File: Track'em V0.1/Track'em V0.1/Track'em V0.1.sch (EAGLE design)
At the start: 34 parts, among them IC1 SAM-M8Q, J1 CORTEX_DEBUG_PTH, U2 3.3V/150mA

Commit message: track'em updates
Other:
- moved on the sheet: C10, C11, C12, C13, C14, C15, C3, C4, C5, C6, C7, C8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

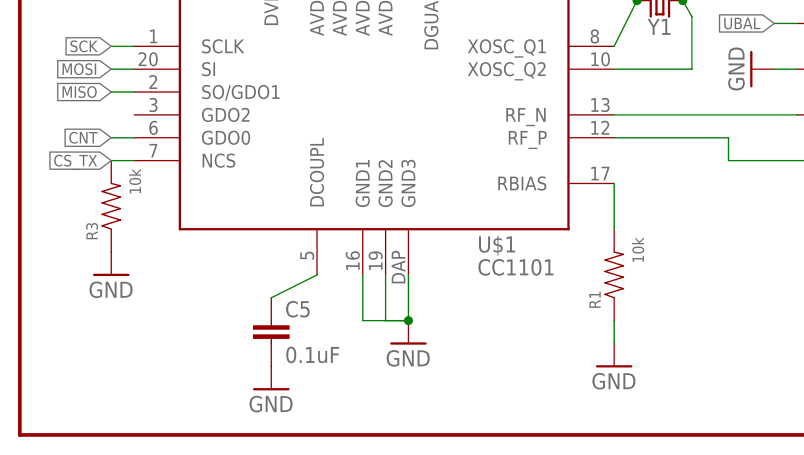
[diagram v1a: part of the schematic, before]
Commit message: boards sent to fab
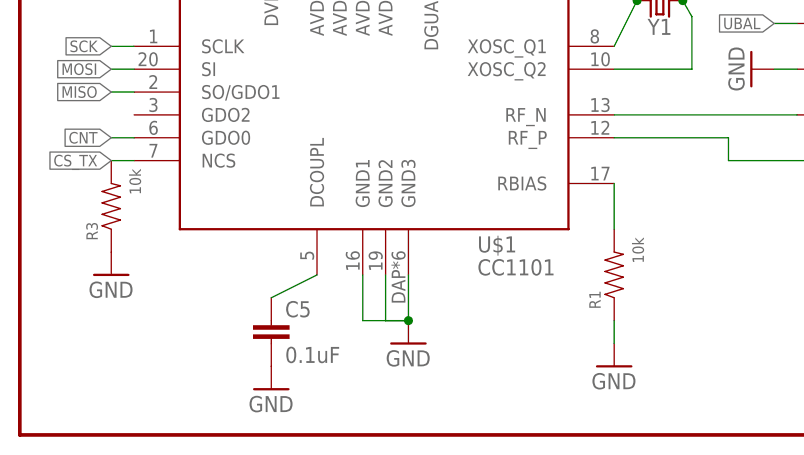
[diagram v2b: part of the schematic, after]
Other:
- moved on the sheet: U$1

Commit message: this Track'em sent to fab
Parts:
- added C16: 10uF, SparkFun-Capacitors:10UF-6.3V-20%(0603)(TANT)"
- C10, C7: value 0.1uF -> 10nF
- C11, C12, C9: value 0.1uF -> 220pF
- C13: value 0.1uF -> 12pF
- C14: value 0.1uF -> 15pF
- C5, C6: value 0.1uF -> 100nF
- R1: value 10k -> 56k
- Y1: value (none) -> 26MHz
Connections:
- net 3.3V: now also C16.+, R3.1
- net GND: now also C16.-; no longer R3.1

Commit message: tracking message parsed from GPS
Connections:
- net USART_RX: now also U$2.PA24(USB_D-/SER1:2); no longer U$2.PA25(USB_D+/SER1:3)
- net USART_TX: now also U$2.PA25(USB_D+/SER1:3); no longer U$2.PA24(USB_D-/SER1:2)
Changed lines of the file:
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@@
 <grid distance="0.1" unitdist="inch" unit="inch" style="lines" multiple="1" display="no" altdistance="0.01" altunitdist="inch" altunit="inch"/>
 <layers>
-<layer number="1" name="Top" color="4" fill="1" visible="yes" active="no"/>
-<layer number="2" name="Route2" color="1" fill="3" visible="yes" active="no"/>
-<layer number="3" name="Route3" color="4" fill="3" visible="yes" active="no"/>
-<layer number="4" name="Route4" color="1" fill="4" visible="yes" active="no"/>
-<layer number="5" name="Route5" color="4" fill="4" visible="yes" active="no"/>
-<layer number="6" name="Route6" color="1" fill="8" visible="yes" active="no"/>
-<layer number="7" name="Route7" color="4" fill="8" visible="yes" active="no"/>
-<layer number="8" name="Route8" color="1" fill="2" visible="yes" active="no"/>
-<layer number="9" name="Route9" color="4" fill="2" visible="yes" active="no"/>
-<layer number="10" name="Route10" color="1" fill="7" visible="yes" active="no"/>
-<layer number="11" name="Route11" color="4" fill="7" visible="yes" active="no"/>
-<layer number="12" name="Route12" color="1" fill="5" visible="yes" active="no"/>
-<layer number="13" name="Route13" color="4" fill="5" visible="yes" active="no"/>
-<layer number="14" name="Route14" color="1" fill="6" visible="yes" active="no"/>
-<layer number="15" name="Route15" color="4" fill="6" visible="yes" active="no"/>
-<layer number="16" name="Bottom" color="1" fill="1" visible="yes" active="no"/>
-<layer number="17" name="Pads" color="2" fill="1" visible="yes" active="no"/>
-<layer number="18" name="Vias" color="2" fill="1" visible="yes" active="no"/>
-<layer number="19" name="Unrouted" color="6" fill="1" visible="yes" active="no"/>
-<layer number="20" name="Dimension" color="24" fill="1" visible="yes" active="no"/>
-<layer number="21" name="tPlace" color="7" fill="1" visible="yes" active="no"/>
-<layer number="22" name="bPlace" color="7" fill="1" visible="yes" active="no"/>
-<layer number="23" name="tOrigins" color="15" fill="1" visible="yes" active="no"/>
-<layer number="24" name="bOrigins" color="15" fill="1" visible="yes" active="no"/>
-<layer number="25" name="tNames" color="7" fill="1" visible="yes" active="no"/>
-<layer number="26" name="bNames" color="7" fill="1" visible="yes" active="no"/>
-<layer number="27" name="tValues" color="7" fill="1" visible="yes" active="no"/>
-<layer number="28" name="bValues" color="7" fill="1" visible="yes" active="no"/>
+<layer number="1" name="Top" color="4" fill="1" visible="no" active="no"/>
+<layer number="2" name="Route2" color="1" fill="3" visible="no" active="no"/>
+<layer number="3" name="Route3" color="4" fill="3" visible="no" active="no"/>
+<layer number="4" name="Route4" color="1" fill="4" visible="no" active="no"/>
+<layer number="5" name="Route5" color="4" fill="4" visible="no" active="no"/>
+<layer number="6" name="Route6" color="1" fill="8" visible="no" active="no"/>
+<layer number="7" name="Route7" color="4" fill="8" visible="no" active="no"/>
+<layer number="8" name="Route8" color="1" fill="2" visible="no" active="no"/>
+<layer number="9" name="Route9" color="4" fill="2" visible="no" active="no"/>
+<layer number="10" name="Route10" color="1" fill="7" visible="no" active="no"/>
+<layer number="11" name="Route11" color="4" fill="7" visible="no" active="no"/>
+<layer number="12" name="Route12" color="1" fill="5" visible="no" active="no"/>
+<layer number="13" name="Route13" color="4" fill="5" visible="no" active="no"/>
+<layer number="14" name="Route14" color="1" fill="6" visible="no" active="no"/>
+<layer number="15" name="Route15" color="4" fill="6" visible="no" active="no"/>
+<layer number="16" name="Bottom" color="1" fill="1" visible="no" active="no"/>
+<layer number="17" name="Pads" color="2" fill="1" visible="no" active="no"/>
+<layer number="18" name="Vias" color="2" fill="1" visible="no" active="no"/>
+<layer number="19" name="Unrouted" color="6" fill="1" visible="no" active="no"/>
+<layer number="20" name="Dimension" color="24" fill="1" visible="no" active="no"/>
+<layer number="21" name="tPlace" color="7" fill="1" visible="no" active="no"/>
+<layer number="22" name="bPlace" color="7" fill="1" visible="no" active="no"/>
+<layer number="23" name="tOrigins" color="15" fill="1" visible="no" active="no"/>
+<layer number="24" name="bOrigins" color="15" fill="1" visible="no" active="no"/>
+<layer number="25" name="tNames" color="7" fill="1" visible="no" active="no"/>
+<layer number="26" name="bNames" color="7" fill="1" visible="no" active="no"/>
+<layer number="27" name="tValues" color="7" fill="1" visible="no" active="no"/>
+<layer number="28" name="bValues" color="7" fill="1" visible="no" active="no"/>
 <layer number="29" name="tStop" color="7" fill="3" visible="no" active="no"/>
 <layer number="30" name="bStop" color="7" fill="6" visible="no" active="no"/>
@@
 <layer number="35" name="tGlue" color="7" fill="4" visible="no" active="no"/>
 <layer number="36" name="bGlue" color="7" fill="5" visible="no" active="no"/>
-<layer number="37" name="tTest" color="7" fill="1" visible="yes" active="no"/>
-<layer number="38" name="bTest" color="7" fill="1" visible="yes" active="no"/>
+<layer number="37" name="tTest" color="7" fill="1" visible="no" active="no"/>
+<layer number="38" name="bTest" color="7" fill="1" visible="no" active="no"/>
 <layer number="39" name="tKeepout" color="4" fill="11" visible="no" active="no"/>
 <layer number="40" name="bKeepout" color="1" fill="11" visible="no" active="no"/>
@@
 <layer number="44" name="Drills" color="7" fill="1" visible="no" active="no"/>
 <layer number="45" name="Holes" color="7" fill="1" visible="no" active="no"/>
-<layer number="46" name="Milling" color="3" fill="1" visible="yes" active="no"/>
-<layer number="47" name="Measures" color="7" fill="1" visible="yes" active="no"/>
-<layer number="48" name="Document" color="7" fill="1" visible="yes" active="no"/>
-<layer number="49" name="Reference" color="7" fill="1" visible="yes" active="no"/>
-<layer number="50" name="dxf" color="7" fill="1" visible="yes" active="no"/>
-<layer number="51" name="tDocu" color="7" fill="1" visible="yes" active="no"/>
-<layer number="52" name="bDocu" color="7" fill="1" visible="yes" active="no"/>
-<layer number="53" name="tGND_GNDA" color="7" fill="9" visible="yes" active="no"/>
-<layer number="54" name="bGND_GNDA" color="1" fill="9" visible="yes" active="no"/>
-<layer number="56" name="wert" color="7" fill="1" visible="yes" active="no"/>
-<layer number="57" name="tCAD" color="7" fill="1" visible="yes" active="no"/>
-<layer number="59" name="tCarbon" color="7" fill="1" visible="yes" active="no"/>
-<layer number="60" name="bCarbon" color="7" fill="1" visible="yes" active="no"/>
+<layer number="46" name="Milling" color="3" fill="1" visible="no" active="no"/>
+<layer number="47" name="Measures" color="7" fill="1" visible="no" active="no"/>
+<layer number="48" name="Document" color="7" fill="1" visible="no" active="no"/>
+<layer number="49" name="Reference" color="7" fill="1" visible="no" active="no"/>
+<layer number="50" name="dxf" color="7" fill="1" visible="no" active="no"/>
+<layer number="51" name="tDocu" color="7" fill="1" visible="no" active="no"/>
+<layer number="52" name="bDocu" color="7" fill="1" visible="no" active="no"/>
+<layer number="53" name="tGND_GNDA" color="7" fill="9" visible="no" active="no"/>
+<layer number="54" name="bGND_GNDA" color="1" fill="9" visible="no" active="no"/>
+<layer number="56" name="wert" color="7" fill="1" visible="no" active="no"/>
+<layer number="57" name="tCAD" color="7" fill="1" visible="no" active="no"/>
+<layer number="59" name="tCarbon" color="7" fill="1" visible="no" active="no"/>
+<layer number="60" name="bCarbon" color="7" fill="1" visible="no" active="no"/>
 <layer number="88" name="SimResults" color="9" fill="1" visible="yes" active="yes"/>
 <layer number="89" name="SimProbes" color="9" fill="1" visible="yes" active="yes"/>
@@
 </segment>
 <segment>
+<pinref part="U$2" gate="G$1" pin="PA24(USB_D-/SER1:2)"/>
+<wire x1="93.98" y1="91.44" x2="91.44" y2="91.44" width="0.1524" layer="91"/>
+<label x="91.44" y="91.44" size="1.27" layer="95" rot="R180" xref="yes"/>
+</segment>
+</net>
+<net name="USART_TX" class="0">
+<segment>
+<pinref part="J1" gate="G$1" pin="NC/TDI"/>
+<wire x1="218.44" y1="134.62" x2="220.98" y2="134.62" width="0.1524" layer="91"/>
+<label x="220.98" y="134.62" size="1.27" layer="95" xref="yes"/>
+</segment>
+<segment>
 <pinref part="U$2" gate="G$1" pin="PA25(USB_D+/SER1:3)"/>
 <wire x1="93.98" y1="93.98" x2="91.44" y2="93.98" width="0.1524" layer="91"/>
@@
 </segment>
 </net>
-<net name="USART_TX" class="0">
-<segment>
-<pinref part="J1" gate="G$1" pin="NC/TDI"/>
-<wire x1="218.44" y1="134.62" x2="220.98" y2="134.62" width="0.1524" layer="91"/>
-<label x="220.98" y="134.62" size="1.27" layer="95" xref="yes"/>
-</segment>
-<segment>
-<pinref part="U$2" gate="G$1" pin="PA24(USB_D-/SER1:2)"/>
-<wire x1="93.98" y1="91.44" x2="91.44" y2="91.44" width="0.1524" layer="91"/>
-<label x="91.44" y="91.44" size="1.27" layer="95" rot="R180" xref="yes"/>
-</segment>
-</net>
